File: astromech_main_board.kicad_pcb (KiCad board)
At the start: 2 copper layers, 124.5 x 129.5 mm, 60 parts, among them IC1 MAX11645EUA+, J1 Screw_Terminal_01x02, J10 Conn_01x05, J11 Conn_01x06, J12 Conn_01x04, J14 Conn_01x04, J19 Conn_01x04, J2 Screw_Terminal_01x02, J20 Conn_01x04, J21 Conn_01x04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

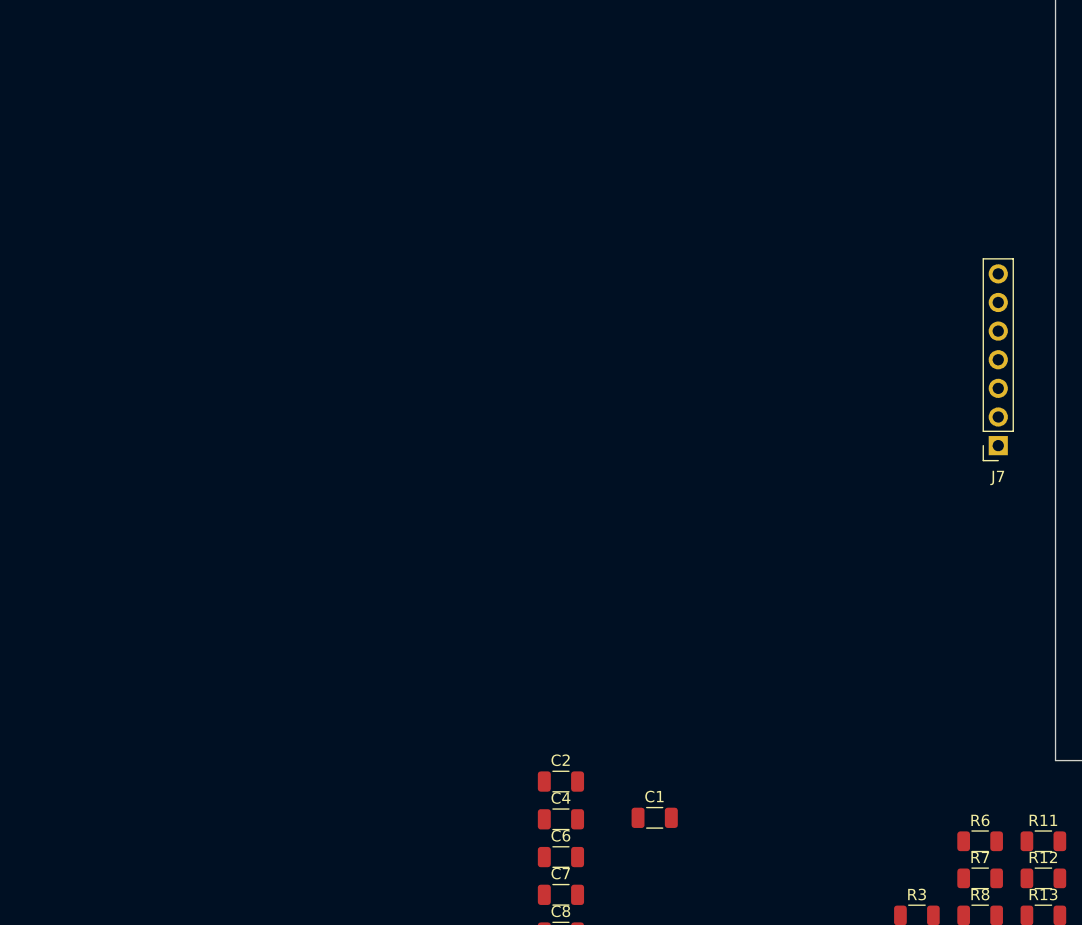
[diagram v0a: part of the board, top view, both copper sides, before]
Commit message: added UART chip
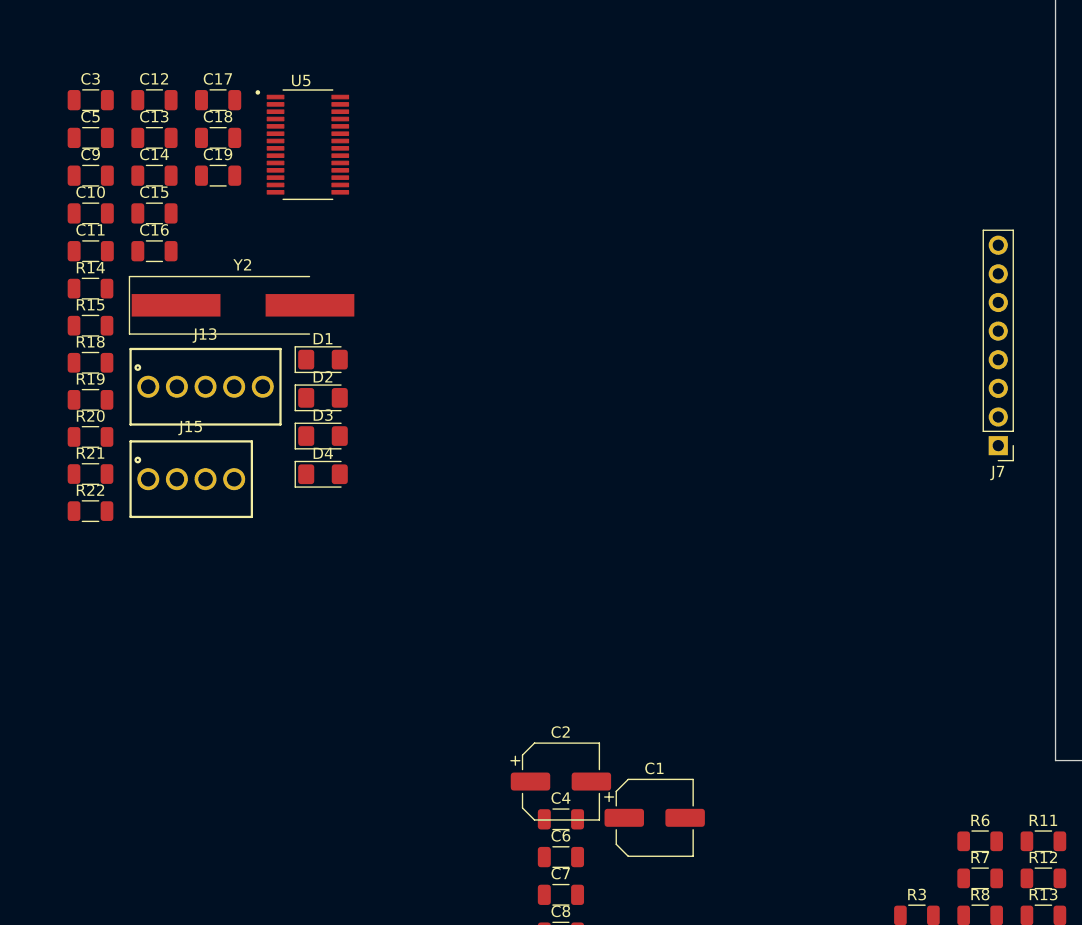
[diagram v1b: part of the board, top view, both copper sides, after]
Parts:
- added C10: C_Small, Capacitor_SMD:C_1206_3216Metric, F.Cu at (64.3, 111.5)
- added C11: C_Small, Capacitor_SMD:C_1206_3216Metric, F.Cu at (64.3, 114.8)
- added C12: C_Small, Capacitor_SMD:C_1206_3216Metric, F.Cu at (69.9, 101.4)
- added C13: C_Small, Capacitor_SMD:C_1206_3216Metric, F.Cu at (69.9, 104.8)
- added C14: C_Small, Capacitor_SMD:C_1206_3216Metric, F.Cu at (69.9, 108.1)
- added C15: C_Small, Capacitor_SMD:C_1206_3216Metric, F.Cu at (69.9, 111.5)
- added C16: C_Small, Capacitor_SMD:C_1206_3216Metric, F.Cu at (69.9, 114.8)
- added C17: C_Small, Capacitor_SMD:C_1206_3216Metric, F.Cu at (75.6, 101.4)
- added C18: C_Small, Capacitor_SMD:C_1206_3216Metric, F.Cu at (75.6, 104.8)
- added C19: C_Small, Capacitor_SMD:C_1206_3216Metric, F.Cu at (75.6, 108.1)
- added C3: C_Small, Capacitor_SMD:C_1206_3216Metric, F.Cu at (64.3, 101.4)
- added C5: C_Small, Capacitor_SMD:C_1206_3216Metric, F.Cu at (64.3, 104.8)
- added C9: C_Small, Capacitor_SMD:C_1206_3216Metric, F.Cu at (64.3, 108.1)
- added D1: LED, LED_SMD:LED_1206_3216Metric_Pad1.42x1.75mm_HandSolder, F.Cu at (84.9, 124.5)
- added D2: LED, LED_SMD:LED_1206_3216Metric_Pad1.42x1.75mm_HandSolder, F.Cu at (84.9, 127.8)
- added D3: LED, LED_SMD:LED_1206_3216Metric_Pad1.42x1.75mm_HandSolder, F.Cu at (84.9, 131.2)
- added D4: LED, LED_SMD:LED_1206_3216Metric_Pad1.42x1.75mm_HandSolder, F.Cu at (84.9, 134.6)
- added J13: Conn_01x05, astromech_footprints:691210910005, F.Cu at (74.5, 126.9)
- added J15: Conn_01x04, astromech_footprints:691210910004, F.Cu at (73.2, 135.1)
- added R14: R_Small_US, Resistor_SMD:R_1206_3216Metric, F.Cu at (64.2, 118.2)
- added R15: R_Small_US, Resistor_SMD:R_1206_3216Metric, F.Cu at (64.2, 121.4)
- added R18: R_Small_US, Resistor_SMD:R_1206_3216Metric, F.Cu at (64.2, 124.7)
- added R19: R_Small_US, Resistor_SMD:R_1206_3216Metric, F.Cu at (64.2, 128.0)
- added R20: R_Small_US, Resistor_SMD:R_1206_3216Metric, F.Cu at (64.2, 131.3)
- added R21: R_Small_US, Resistor_SMD:R_1206_3216Metric, F.Cu at (64.2, 134.6)
- added R22: R_Small_US, Resistor_SMD:R_1206_3216Metric, F.Cu at (64.2, 137.9)
- added U5: SC16IS752IPW_128, astromech_footprints:SOP65P640X110-28N, F.Cu at (83.5, 105.4)
- added Y2: Crystal, Crystal:Crystal_SMD_HC49-SD_HandSoldering, F.Cu at (77.8, 119.6)
- C1, C2: footprint Capacitor_SMD:C_1206_3216Metric -> Capacitor_SMD:CP_Elec_6.3x5.8
- J7: value Conn_01x07 -> Conn_01x08; footprint Connector_PinSocket_2.54mm:PinSocket_1x07_P2.54mm_Vertical -> Connector_PinHeader_2.54mm:PinHeader_1x08_P2.54mm_Vertical
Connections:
- J14 pad 2: /IO17 -> /UART_TXA
- J14 pad 3: /IO8 -> /UART_RXA
- J7 pad 1: /IO14 -> /IO17
- J7 pad 2: /IO21 -> /IO8
- J7 pad 3: /IO35 -> /IO21
- J7 pad 4: /IO40 -> /IO35
- J7 pad 5: /IO45 -> /IO40
- J7 pad 6: /IOTX -> /IO45
- J7 pad 7: /IORX -> /IOTX

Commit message: started routing
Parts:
- IC1, U3, U4: moved to B.Cu
- moved J13 195.1 mm to (264.2, 81.3), turned to -90 degrees
- moved C1 144.0 mm to (199.1, 48.8)
- moved C2 138.8 mm to (199.1, 58.9)
- moved Y2 106.1 mm to (177.8, 154.9)
- moved U5 94.5 mm to (172.2, 138.2)
- moved J15 86.9 mm to (160.0, 130.8), turned to 90 degrees
- moved R10 63.5 mm to (80.3, 170.9)
- moved R6 63.5 mm to (80.3, 157.8)
- moved R7 63.5 mm to (80.3, 161.1)
- moved R8 63.5 mm to (80.3, 164.3)
- moved R9 63.5 mm to (80.3, 167.6)
- moved C4 63.5 mm to (43.2, 155.8)
- moved C6 63.5 mm to (43.2, 159.2)
- moved C7 63.5 mm to (43.2, 162.5)
- moved C8 63.5 mm to (43.2, 165.9)
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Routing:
- net Net-(IC1-AIN0): track 0.00 -> 9.38 mm, vias 0 -> 1
- net /VBAT: track 0.00 -> 9.14 mm
- net Net-(MCU_3V3-Pad1): track 0.00 -> 5.14 mm
- net Net-(JP8-B): track 0.00 -> 4.29 mm, vias 0 -> 1
- net 5V: vias 0 -> 6
- added copper zone on F.Cu, net /3V3_IN
- added copper zone on F.Cu, net /5V_IN
- added copper zone on F.Cu, net 5V
- added copper zone on F.Cu, net GND
- added copper zone on F.Cu, net Net-(J1-Pin_1)
- added copper zone on F.Cu, net Net-(J2-Pin_1)

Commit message: layout mostly done
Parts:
- removed R7: R_Small_US, Resistor_SMD:R_1206_3216Metric
- C10, C11, C12, C14, C15, C16, C3, C4, C5, C6, R10, R11, R13, R16, R17, R20, R21, R22, R3, R4, R8, R9, U6: moved to B.Cu
- moved H2 213.2 mm to (242.6, 49.5)
- moved C6 194.2 mm to (236.2, 138.4), turned to 90 degrees
- moved R5 188.2 mm to (238.8, 78.7), turned to 180 degrees
- moved H4 182.1 mm to (242.6, 142.2)
- moved C4 181.3 mm to (223.5, 137.8), turned to 180 degrees
- moved J7 181.2 mm to (220.5, -32.5)
- moved R6 175.4 mm to (238.8, 82.5), turned to 180 degrees
- moved C8 168.8 mm to (201.6, 107.8), turned to -90 degrees
- moved C11 168.2 mm to (232.4, 119.6), turned to 90 degrees
- moved C10 168.2 mm to (232.4, 109.4), turned to 90 degrees
- moved C12 164.9 mm to (232.4, 129.7), turned to 90 degrees
- moved H1 164.1 mm to (135.9, 48.3)
- moved C7 164.0 mm to (201.6, 120.5), turned to 90 degrees
- moved R13 159.0 mm to (233.7, 105.4)
- moved C9 151.3 mm to (214.0, 130.2), turned to -90 degrees
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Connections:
- C10 pad 2: 5V -> 3V3
- C11 pad 2: 5V -> 3V3
- C12 pad 2: 5V -> 3V3
- R14 pad 1: Net-(J4-Pin_13) -> Net-(J4-Pin_4)
- R15 pad 1: Net-(J4-Pin_14) -> Net-(J4-Pin_3)
- R18 pad 1: Net-(J4-Pin_15) -> Net-(J4-Pin_2)
- R19 pad 1: Net-(J4-Pin_16) -> Net-(J4-Pin_1)
- R22 pad 1: 3V3 -> /IO14
- R22 pad 2: /IO14 -> 3V3
- U10 pad 14: 5V -> 3V3
- U11 pad 14: 5V -> 3V3
- U8 pad 12: unconnected-(U8-Pad12) -> /IO18
- U8 pad 13: unconnected-(U8-Pad13) -> Net-(JP13-B)
- U8 pad 3: Net-(JP13-B) -> unconnected-(U8-Pad3)
- U8 pad 4: /IO18 -> unconnected-(U8-Pad4)
- U9 pad 14: 5V -> 3V3
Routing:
- net 5V: track 0.00 -> 234.1 mm
- net /I2C_3V3_SCL: track 0.00 -> 137.8 mm, vias 0 -> 7
- net /I2C_3V3_SDA: track 0.00 -> 133.9 mm, vias 0 -> 7
- net /IO4: track 0.00 -> 114.8 mm, vias 0 -> 1
- net /IO3: track 0.00 -> 113.9 mm, vias 0 -> 1
- net /IO0: track 0.00 -> 111.2 mm, vias 0 -> 1
- net /IO2: track 0.00 -> 109.9 mm, vias 0 -> 1
- net /IO1: track 0.00 -> 107.3 mm, vias 0 -> 1
- net /IO36: track 0.00 -> 103.6 mm, vias 0 -> 1
- net /IO39: track 0.00 -> 102.4 mm, vias 0 -> 1
- net /IO38: track 0.00 -> 101.1 mm, vias 0 -> 1
- net /IO37: track 0.00 -> 100.3 mm, vias 0 -> 1
- net /RST: track 0.00 -> 84.2 mm, vias 0 -> 1
- net /IO14: track 0.00 -> 78.3 mm, vias 0 -> 2
- net /IO10: track 0.00 -> 77.0 mm, vias 0 -> 1
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- added copper zone on B.Cu, net 3V3
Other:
- board size 124.5 x 129.5 mm -> 100.3 x 109.2 mm

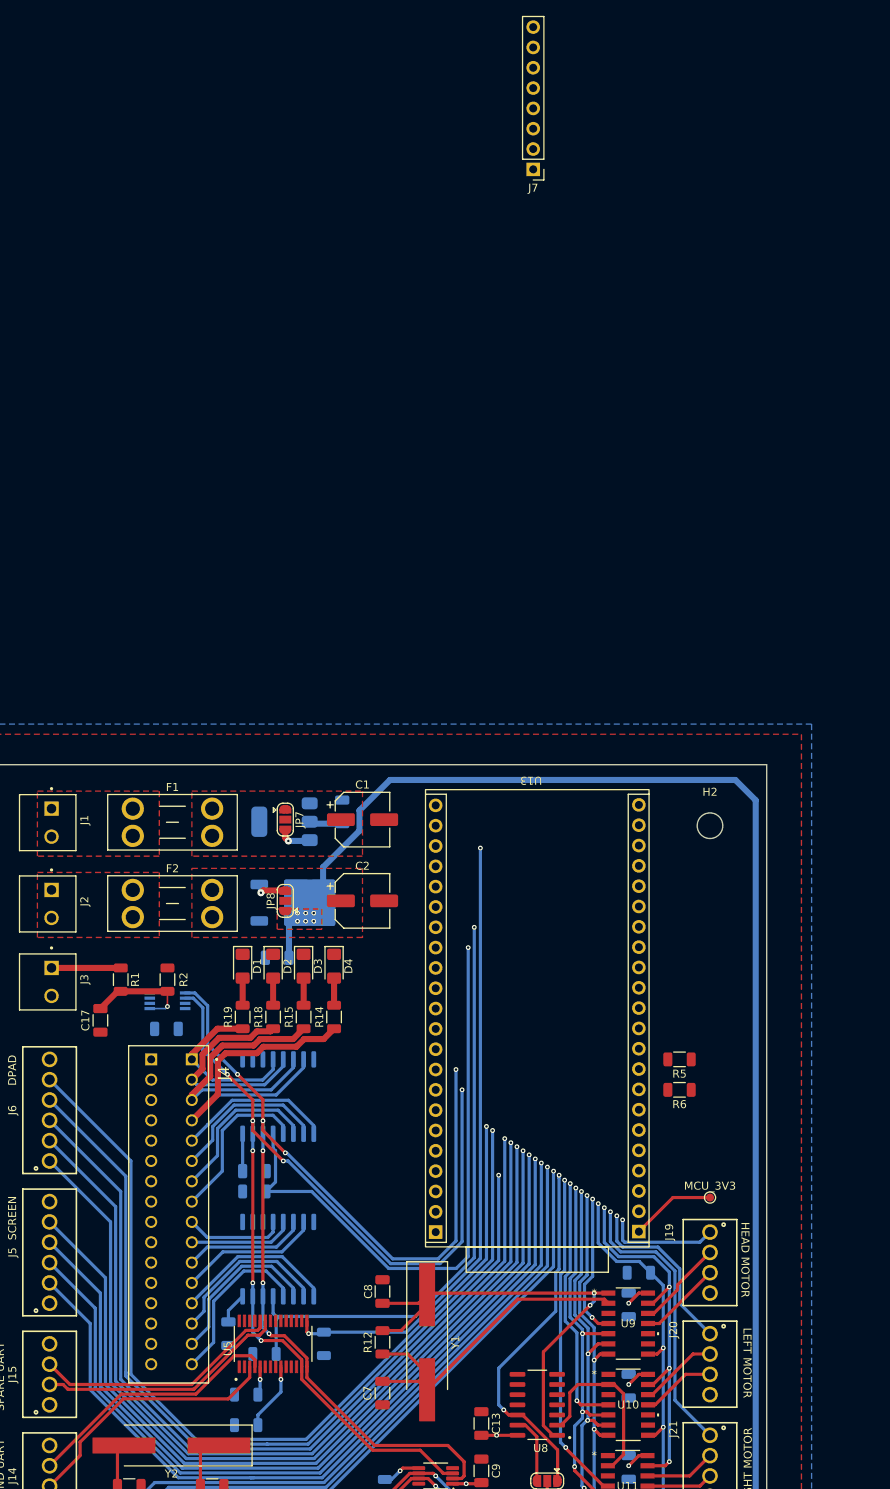
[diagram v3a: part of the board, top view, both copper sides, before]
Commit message: main routing done
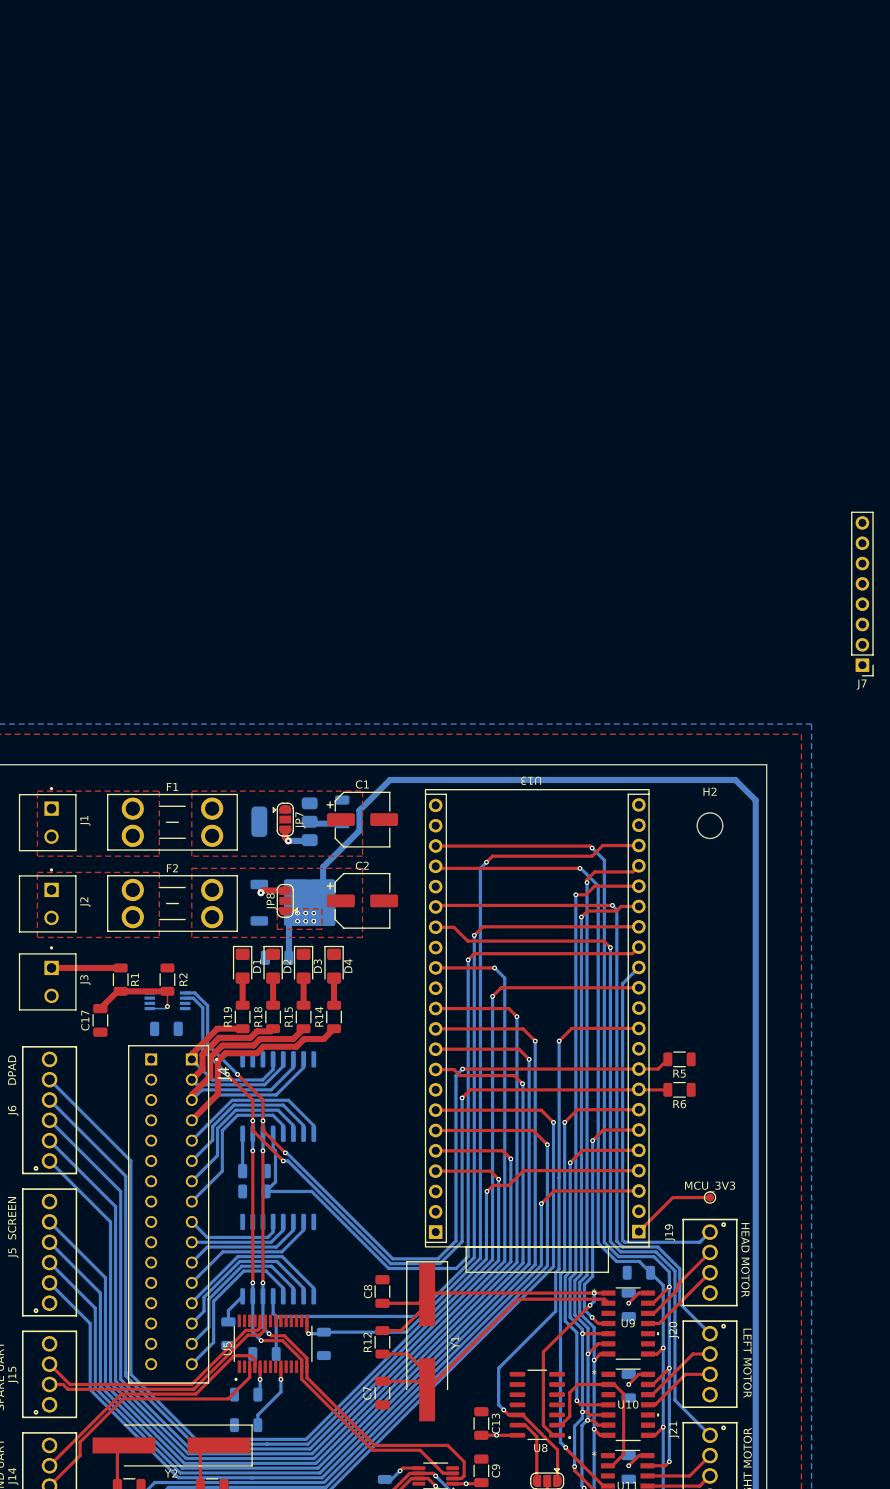
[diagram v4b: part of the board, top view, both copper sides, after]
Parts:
- moved J7 74.4 mm to (261.6, 29.5)
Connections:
- R17 pad 1: /IO40 -> /IO42
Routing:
- net /IO42: track 0.00 -> 91.8 mm, vias 0 -> 1
- net /IO40: track 74.3 -> 0.00 mm, vias 1 -> 0
- net /ENC_CNT_EN: track 47.7 -> 112.9 mm
- net /IO47: track 22.1 -> 83.3 mm
- net /ENC_INT: track 50.4 -> 111.4 mm
- net /IO48: track 35.7 -> 91.6 mm
- net /IO13: track 47.3 -> 94.0 mm
- net /IO12: track 48.8 -> 93.8 mm
- net /IO11: track 48.4 -> 90.4 mm
- net /IO3: track 113.9 -> 149.4 mm
- net /IO46: track 14.1 -> 46.5 mm, vias 1 -> 0
- net /IO0: track 111.2 -> 140.4 mm
- net /IO37: track 100.3 -> 128.1 mm
- net /IO18: track 45.4 -> 72.8 mm
- net /IO36: track 103.6 -> 130.4 mm
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
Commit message: 3v3 routed
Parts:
- moved J7 41.5 mm to (244.6, 67.3), turned to 0 degrees
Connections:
- J7 pad 1: /IO17 -> /IO21
- J7 pad 2: /IO8 -> /IO45
- J7 pad 3: /IO21 -> /IO35
- J7 pad 4: /IO35 -> /IO8
- J7 pad 5: /IO40 -> /IO17
- J7 pad 6: /IO45 -> /IO40
- J7 pad 7: /IOTX -> /IORX
- J7 pad 8: /IORX -> /IOTX
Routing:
- net /IORX: track 0.00 -> 43.4 mm
- net /IOTX: track 0.00 -> 42.3 mm
- net /IO21: track 0.00 -> 40.9 mm
- net /IO45: track 0.00 -> 38.4 mm
- net /IO35: track 0.00 -> 37.8 mm
- net /IO40: track 0.00 -> 37.4 mm
- net GND: track 0.00 -> 25.1 mm, vias 0 -> 6
- net 3V3: track 29.1 -> 48.5 mm, vias 5 -> 12
- net /IO8: track 0.00 -> 12.0 mm
- net /IO17: track 0.00 -> 11.7 mm
- net 5V: track 234.1 -> 242.0 mm, vias 6 -> 7
- net Net-(JP8-B): track 4.29 -> 5.36 mm
